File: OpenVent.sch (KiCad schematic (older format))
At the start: 0 parts

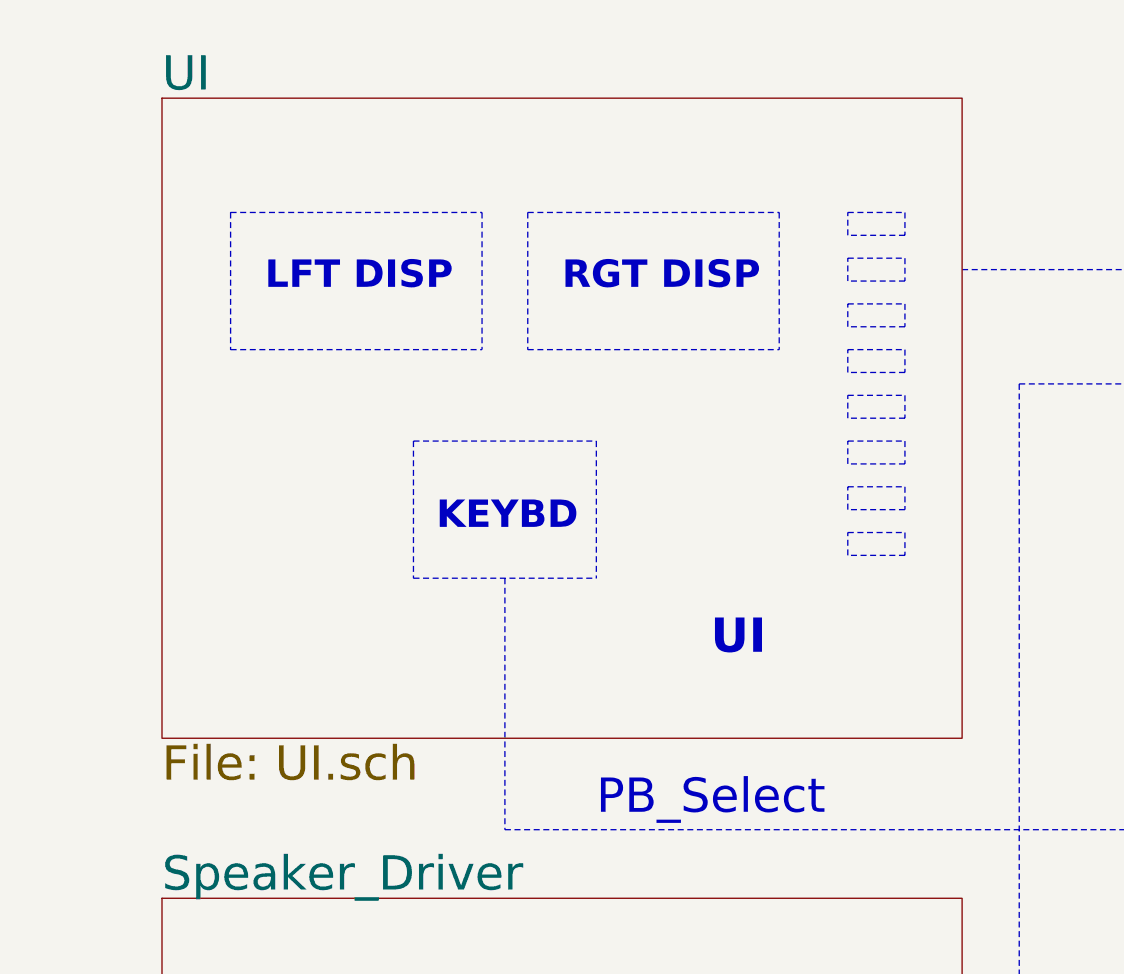
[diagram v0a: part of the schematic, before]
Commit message: Task OEF-623
Split LCD and serial LEDs onto separate sheet as UI too full. Separated the decoupling capacitors from the serial LED for the second time to make schematic clearer. Added 74AHCT1G86 XOR gate to LED drive signal
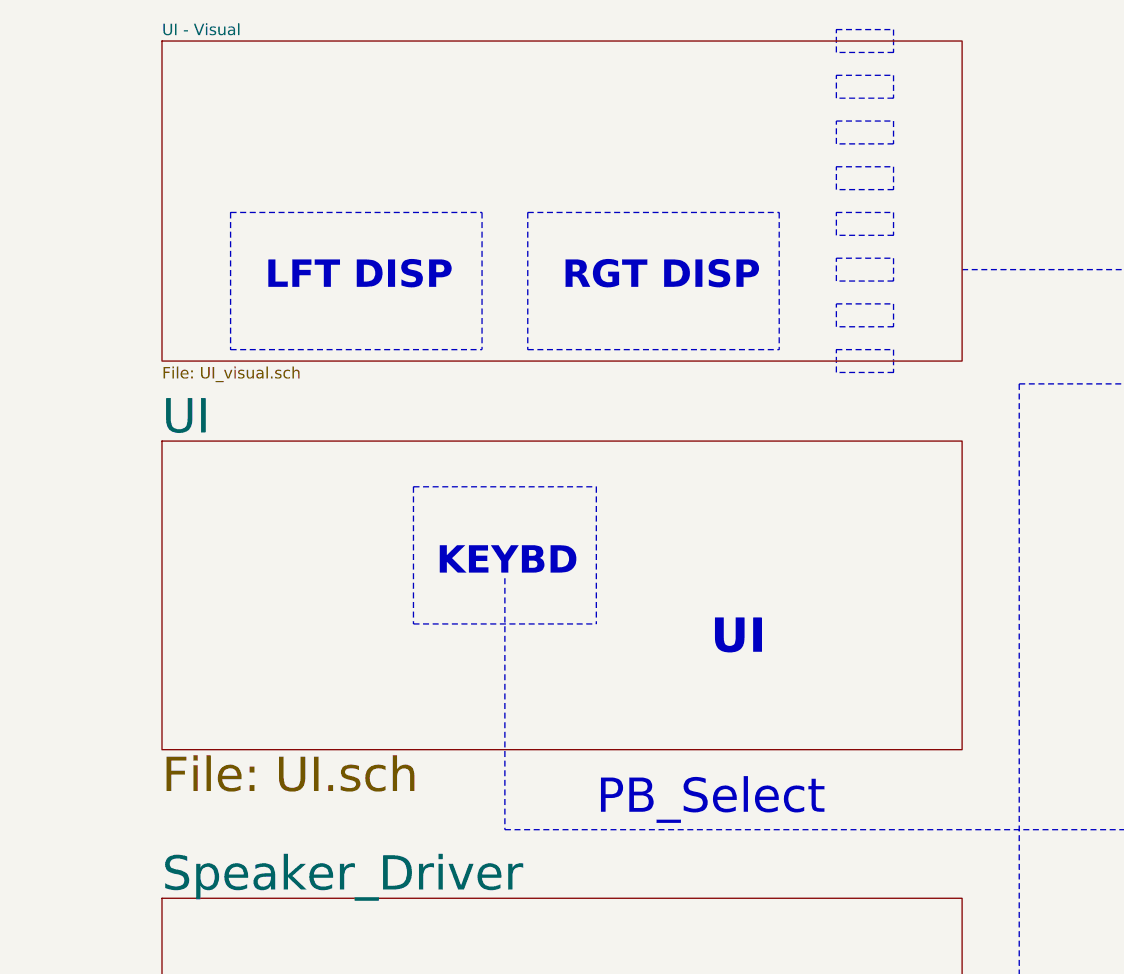
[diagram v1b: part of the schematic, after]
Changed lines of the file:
@@
 $Descr A3 16535 11693
 encoding utf-8
-Sheet 1 9
+Sheet 1 10
 Title "OpenVent Control Board"
 Date "2020-10-20"
@@
 LFT DISP
 Wire Notes Line width 20 style solid
-	3400 2500 3400 3100
-Wire Notes Line width 20 style solid
-	2600 2500 2600 3100
-Wire Notes Line width 20 style solid
-	2600 3100 3400 3100
-Text Notes 2700 2900 0    120  ~ 24
+	3400 2700 3400 3300
+Wire Notes Line width 20 style solid
+	2600 2700 2600 3300
+Wire Notes Line width 20 style solid
+	2600 3300 3400 3300
+Text Notes 2700 3100 0    120  ~ 24
 KEYBD
 Text Notes 3250 1850 0    120  ~ 24
@@
 	5000 1750 7000 1750
 Wire Notes Line width 20 style solid
-	2600 2500 3400 2500
+	2600 2700 3400 2700
 Wire Notes Line width 12 style solid
 	8000 3650 8000 8250
-Wire Notes Line width 12 style solid
-	3000 3100 3000 4200
 Text Notes 3400 4150 0    150  ~ 0
 PB_Select
@@
 	12800 8150 12800 9150
 Wire Notes Line
-	4500 3000 4500 2900
-Wire Notes Line
-	4750 3000 4500 3000
-Wire Notes Line
-	4750 2900 4750 3000
-Wire Notes Line
-	4500 2900 4750 2900
-Wire Notes Line
-	4500 2800 4500 2700
-Wire Notes Line
-	4750 2800 4500 2800
-Wire Notes Line
-	4750 2700 4750 2800
-Wire Notes Line
-	4500 2700 4750 2700
-Wire Notes Line
-	4500 2600 4500 2500
-Wire Notes Line
-	4750 2600 4500 2600
-Wire Notes Line
-	4750 2500 4750 2600
-Wire Notes Line
-	4500 2500 4750 2500
-Wire Notes Line
-	4500 2400 4500 2300
-Wire Notes Line
-	4750 2400 4500 2400
-Wire Notes Line
-	4750 2300 4750 2400
-Wire Notes Line
-	4500 2300 4750 2300
-Wire Notes Line
-	4500 2200 4500 2100
-Wire Notes Line
-	4750 2200 4500 2200
-Wire Notes Line
-	4750 2100 4750 2200
-Wire Notes Line
-	4500 2100 4750 2100
-Wire Notes Line
-	4500 2000 4500 1900
-Wire Notes Line
-	4750 2000 4500 2000
-Wire Notes Line
-	4750 1900 4750 2000
-Wire Notes Line
-	4500 1900 4750 1900
-Wire Notes Line
-	4500 1800 4500 1700
-Wire Notes Line
-	4750 1800 4500 1800
-Wire Notes Line
-	4750 1700 4750 1800
-Wire Notes Line
-	4500 1700 4750 1700
-Wire Notes Line
-	4500 1600 4500 1500
-Wire Notes Line
-	4750 1600 4500 1600
-Wire Notes Line
-	4750 1500 4750 1600
-Wire Notes Line
-	4500 1500 4750 1500
+	4450 2200 4450 2100
+Wire Notes Line
+	4700 2200 4450 2200
+Wire Notes Line
+	4700 2100 4700 2200
+Wire Notes Line
+	4450 2100 4700 2100
+Wire Notes Line
+	4450 2000 4450 1900
+Wire Notes Line
+	4700 2000 4450 2000
+Wire Notes Line
+	4700 1900 4700 2000
+Wire Notes Line
+	4450 1900 4700 1900
+Wire Notes Line
+	4450 1800 4450 1700
+Wire Notes Line
+	4700 1800 4450 1800
+Wire Notes Line
+	4700 1700 4700 1800
+Wire Notes Line
+	4450 1700 4700 1700
+Wire Notes Line
+	4450 1600 4450 1500
+Wire Notes Line
+	4700 1600 4450 1600
+Wire Notes Line
+	4700 1500 4700 1600
+Wire Notes Line
+	4450 1500 4700 1500
+Wire Notes Line
+	4450 1400 4450 1300
+Wire Notes Line
+	4700 1400 4450 1400
+Wire Notes Line
+	4700 1300 4700 1400
+Wire Notes Line
+	4450 1300 4700 1300
+Wire Notes Line
+	4450 1200 4450 1100
+Wire Notes Line
+	4700 1200 4450 1200
+Wire Notes Line
+	4700 1100 4700 1200
+Wire Notes Line
+	4450 1100 4700 1100
+Wire Notes Line
+	4450 1000 4450 900
+Wire Notes Line
+	4700 1000 4450 1000
+Wire Notes Line
+	4700 900  4700 1000
+Wire Notes Line
+	4450 900  4700 900
+Wire Notes Line
+	4450 800  4450 700
+Wire Notes Line
+	4700 800  4450 800
+Wire Notes Line
+	4700 700  4700 800
+Wire Notes Line
+	4450 700  4700 700
 Wire Notes Line width 12 style solid
 	15500 8650 15750 8650
@@
 $EndSheet
 $Sheet
-S 1500 1000 3500 2800
+S 1500 2500 3500 1350
 U 5FCA4074
 F0 "UI" 150
@@
 F1 "Power_Supplies.sch" 150
 $EndSheet
+$Sheet
+S 1500 750  3500 1400
+U 6092237A
+F0 "UI - Visual" 50
+F1 "UI_visual.sch" 50
+$EndSheet
+Wire Notes Line width 12 style solid
+	3000 3100 3000 4200
 $EndSCHEMATC

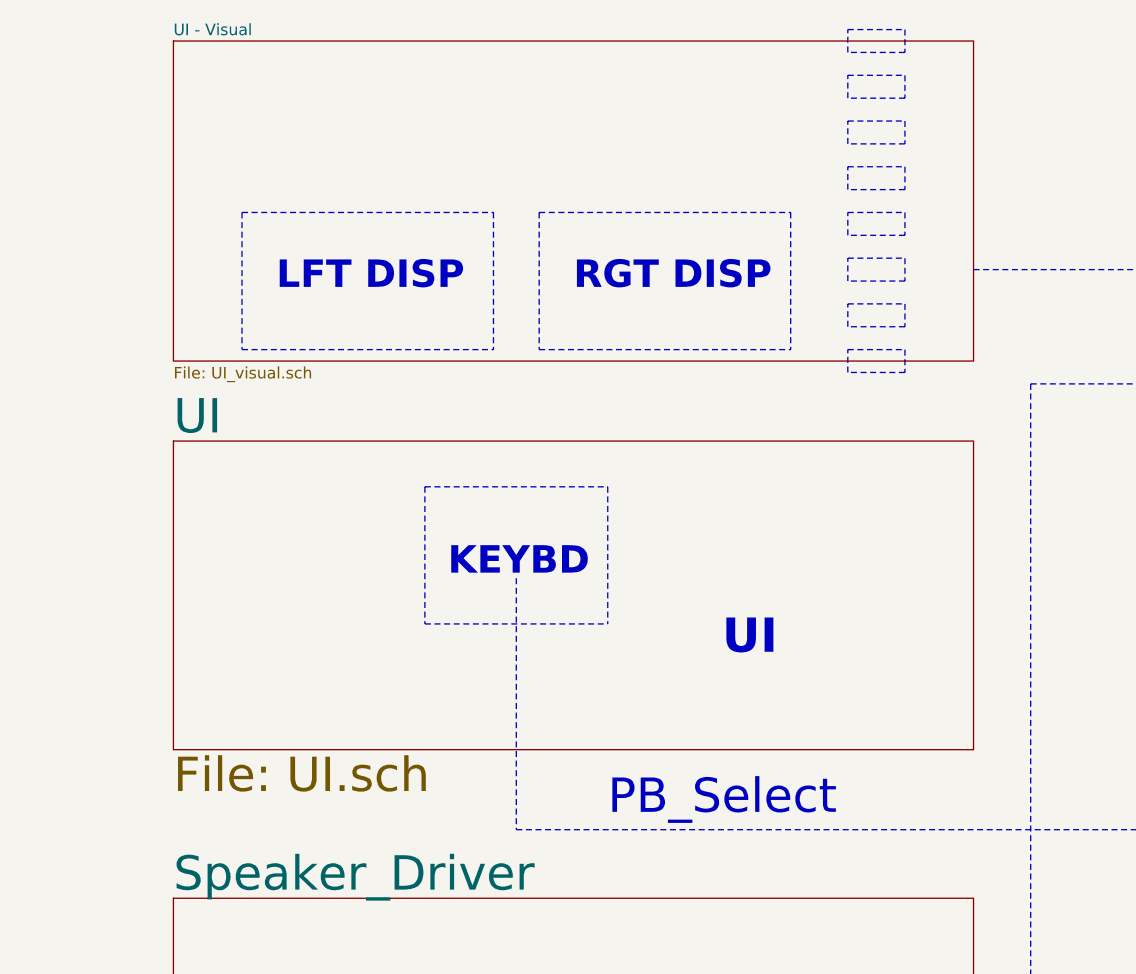
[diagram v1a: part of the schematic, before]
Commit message: Merged Rick's UI
Merged in Rick's copy of UI page (speaker circuit deleted, removing need for separate UI-visual sheet)
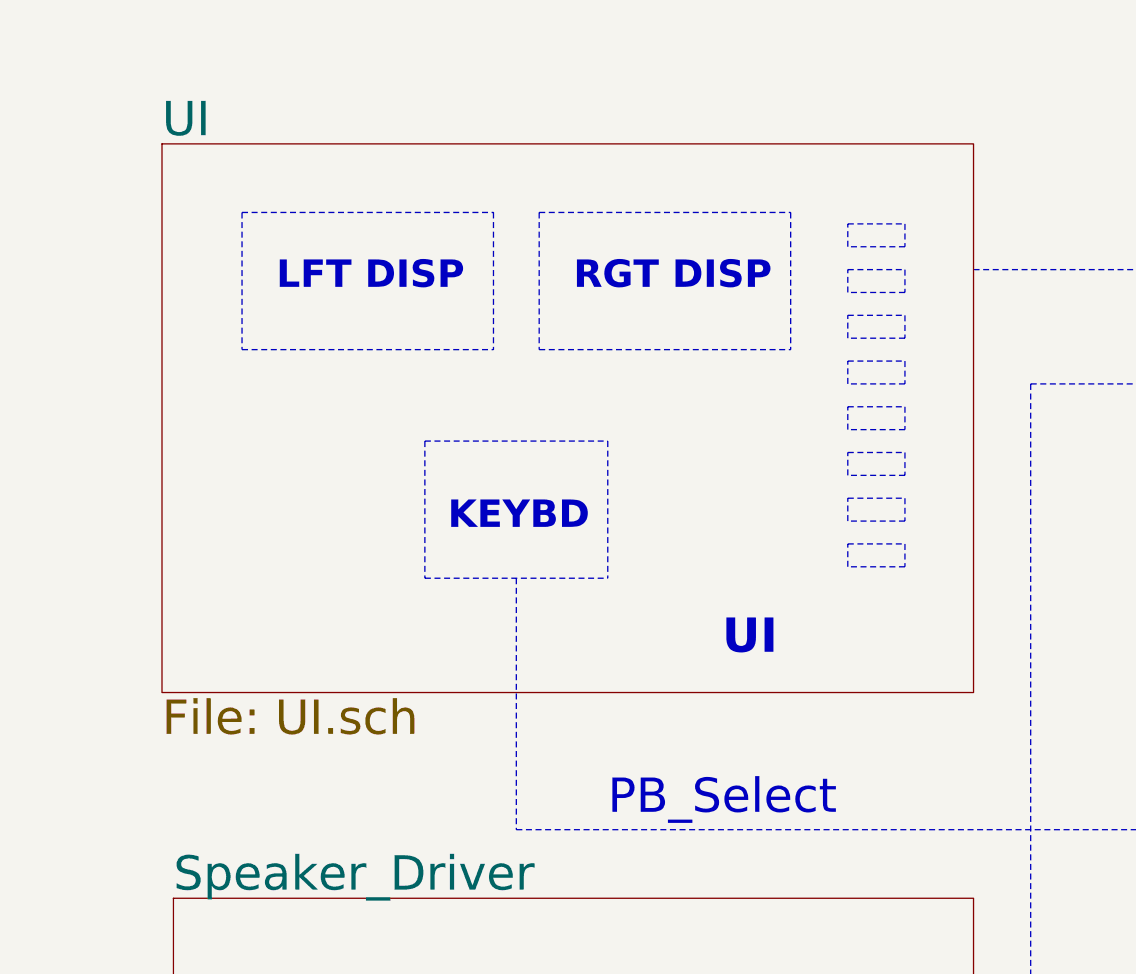
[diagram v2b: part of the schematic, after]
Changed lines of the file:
@@
 $Descr A3 16535 11693
 encoding utf-8
-Sheet 1 10
+Sheet 1 9
 Title "OpenVent Control Board"
 Date "2020-10-20"
@@
 LFT DISP
 Wire Notes Line width 20 style solid
-	3400 2700 3400 3300
-Wire Notes Line width 20 style solid
-	2600 2700 2600 3300
-Wire Notes Line width 20 style solid
-	2600 3300 3400 3300
-Text Notes 2700 3100 0    120  ~ 24
+	3400 2500 3400 3100
+Wire Notes Line width 20 style solid
+	2600 2500 2600 3100
+Wire Notes Line width 20 style solid
+	2600 3100 3400 3100
+Text Notes 2700 2900 0    120  ~ 24
 KEYBD
 Text Notes 3250 1850 0    120  ~ 24
@@
 	5000 1750 7000 1750
 Wire Notes Line width 20 style solid
-	2600 2700 3400 2700
+	2600 2500 3400 2500
 Wire Notes Line width 12 style solid
 	8000 3650 8000 8250
@@
 	12800 8150 12800 9150
 Wire Notes Line
-	4450 2200 4450 2100
-Wire Notes Line
-	4700 2200 4450 2200
-Wire Notes Line
-	4700 2100 4700 2200
-Wire Notes Line
-	4450 2100 4700 2100
-Wire Notes Line
-	4450 2000 4450 1900
-Wire Notes Line
-	4700 2000 4450 2000
-Wire Notes Line
-	4700 1900 4700 2000
-Wire Notes Line
-	4450 1900 4700 1900
-Wire Notes Line
-	4450 1800 4450 1700
-Wire Notes Line
-	4700 1800 4450 1800
-Wire Notes Line
-	4700 1700 4700 1800
-Wire Notes Line
-	4450 1700 4700 1700
-Wire Notes Line
-	4450 1600 4450 1500
-Wire Notes Line
-	4700 1600 4450 1600
-Wire Notes Line
-	4700 1500 4700 1600
-Wire Notes Line
-	4450 1500 4700 1500
-Wire Notes Line
-	4450 1400 4450 1300
-Wire Notes Line
-	4700 1400 4450 1400
-Wire Notes Line
-	4700 1300 4700 1400
-Wire Notes Line
-	4450 1300 4700 1300
-Wire Notes Line
-	4450 1200 4450 1100
-Wire Notes Line
-	4700 1200 4450 1200
-Wire Notes Line
-	4700 1100 4700 1200
-Wire Notes Line
-	4450 1100 4700 1100
-Wire Notes Line
-	4450 1000 4450 900
-Wire Notes Line
-	4700 1000 4450 1000
-Wire Notes Line
-	4700 900  4700 1000
-Wire Notes Line
-	4450 900  4700 900
-Wire Notes Line
-	4450 800  4450 700
-Wire Notes Line
-	4700 800  4450 800
-Wire Notes Line
-	4700 700  4700 800
-Wire Notes Line
-	4450 700  4700 700
+	4450 3050 4450 2950
+Wire Notes Line
+	4700 3050 4450 3050
+Wire Notes Line
+	4700 2950 4700 3050
+Wire Notes Line
+	4450 2950 4700 2950
+Wire Notes Line
+	4450 2850 4450 2750
+Wire Notes Line
+	4700 2850 4450 2850
+Wire Notes Line
+	4700 2750 4700 2850
+Wire Notes Line
+	4450 2750 4700 2750
+Wire Notes Line
+	4450 2650 4450 2550
+Wire Notes Line
+	4700 2650 4450 2650
+Wire Notes Line
+	4700 2550 4700 2650
+Wire Notes Line
+	4450 2550 4700 2550
+Wire Notes Line
+	4450 2450 4450 2350
+Wire Notes Line
+	4700 2450 4450 2450
+Wire Notes Line
+	4700 2350 4700 2450
+Wire Notes Line
+	4450 2350 4700 2350
+Wire Notes Line
+	4450 2250 4450 2150
+Wire Notes Line
+	4700 2250 4450 2250
+Wire Notes Line
+	4700 2150 4700 2250
+Wire Notes Line
+	4450 2150 4700 2150
+Wire Notes Line
+	4450 2050 4450 1950
+Wire Notes Line
+	4700 2050 4450 2050
+Wire Notes Line
+	4700 1950 4700 2050
+Wire Notes Line
+	4450 1950 4700 1950
+Wire Notes Line
+	4450 1850 4450 1750
+Wire Notes Line
+	4700 1850 4450 1850
+Wire Notes Line
+	4700 1750 4700 1850
+Wire Notes Line
+	4450 1750 4700 1750
+Wire Notes Line
+	4450 1650 4450 1550
+Wire Notes Line
+	4700 1650 4450 1650
+Wire Notes Line
+	4700 1550 4700 1650
+Wire Notes Line
+	4450 1550 4700 1550
 Wire Notes Line width 12 style solid
 	15500 8650 15750 8650
@@
 $EndSheet
 $Sheet
-S 1500 2500 3500 1350
+S 1450 1200 3550 2400
 U 5FCA4074
 F0 "UI" 150
@@
 F1 "Power_Supplies.sch" 150
 $EndSheet
-$Sheet
-S 1500 750  3500 1400
-U 6092237A
-F0 "UI - Visual" 50
-F1 "UI_visual.sch" 50
-$EndSheet
-Wire Notes Line width 12 style solid
+Wire Notes Line width 12 style solid

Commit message: Rick's changes - April 19
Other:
- note added: "Flow"
- note added: "nRST"
- note removed: "SWD"
